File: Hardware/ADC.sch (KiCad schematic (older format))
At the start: 9 parts, among them U2 NCP51460SN33T1G, U3 MCP3002

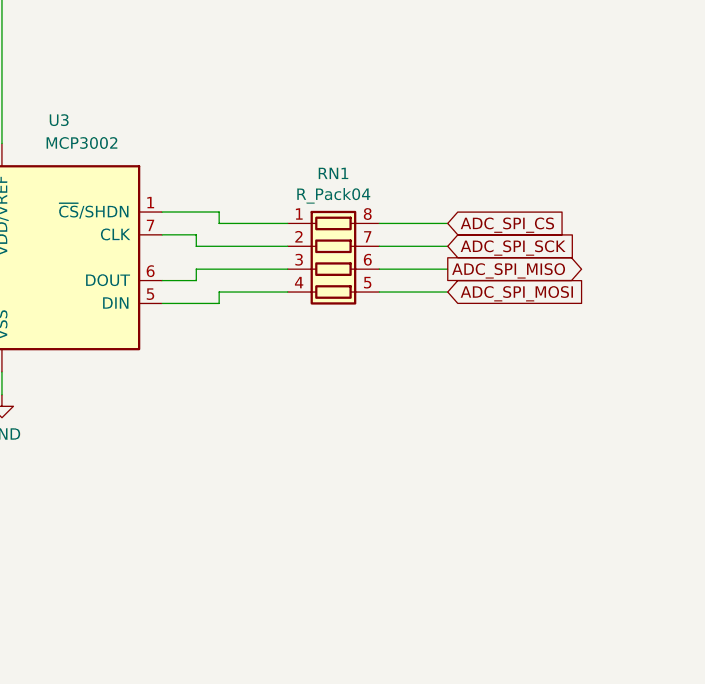
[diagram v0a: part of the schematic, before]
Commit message: [Hardware] Replaced in schematic hard to find resistors array using 2012 package by classic 1206 discrete resistors.
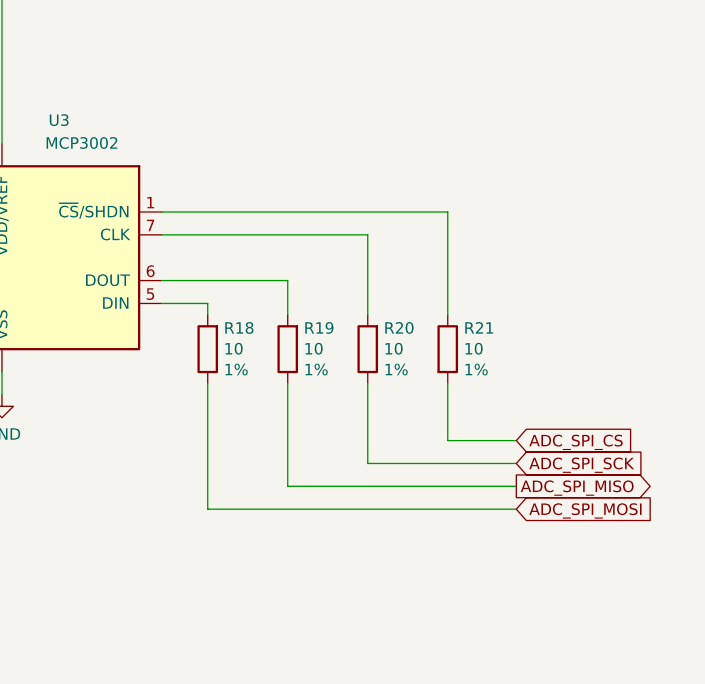
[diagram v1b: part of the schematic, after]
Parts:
- removed RN1: R_Pack04, Resistor_SMD:R_Array_Convex_4x1206, symbol Device:R_Pack04
- added R18, R19, R20, R21: 10, Resistor_SMD:R_1206_3216Metric_Pad1.42x1.75mm_HandSolder, symbol Device:R
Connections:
- net ADC_SPI_CS: now also R21.2
- net ADC_SPI_MISO: now also R19.1
- net ADC_SPI_MOSI: now also R18.1
- net ADC_SPI_SCK: now also R20.1
- net at U3.1 (~CS~/SHDN): now also R21.1
- net at U3.7 (CLK): now also R20.2
- net at U3.6 (DOUT): now also R19.2
- net at U3.5 (DIN): now also R18.2
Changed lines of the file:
@@
 Wire Wire Line
 	6000 4200 6000 4100
-Text GLabel 7950 3450 2    50   Input ~ 0
+Text GLabel 8250 4400 2    50   Input ~ 0
 ADC_SPI_CS
-Text GLabel 7950 3550 2    50   Input ~ 0
+Text GLabel 8250 4500 2    50   Input ~ 0
 ADC_SPI_SCK
-Text GLabel 7950 3650 2    50   Output ~ 0
+Text GLabel 8250 4600 2    50   Output ~ 0
 ADC_SPI_MISO
-Text GLabel 7950 3750 2    50   Input ~ 0
+Text GLabel 8250 4700 2    50   Input ~ 0
 ADC_SPI_MOSI
 $Comp
@@
 Wire Wire Line
 	3700 5250 3700 5200
-$Comp
-L Device:R_Pack04 RN1
-U 1 1 5F207575
-P 7450 3650
-F 0 "RN1" V 7033 3650 50  0000 C CNN
-F 1 "R_Pack04" V 7124 3650 50  0000 C CNN
-F 2 "Resistor_SMD:R_Array_Convex_4x1206" V 7725 3650 50  0001 C CNN
-F 3 "~" H 7450 3650 50  0001 C CNN
-F 4 "MP000987" V 7450 3650 50  0001 C CNN "Value2"
-F 5 "Multicomp" V 7450 3650 50  0001 C CNN "Manufacturer"
-	1    7450 3650
-	0    1    1    0
-$EndComp
-Wire Wire Line
-	6700 3700 6850 3700
-Wire Wire Line
-	6850 3700 6850 3650
-Wire Wire Line
-	6850 3650 7250 3650
-Wire Wire Line
-	6950 3800 6950 3750
-Wire Wire Line
-	6950 3750 7250 3750
-Wire Wire Line
-	6700 3800 6950 3800
-Wire Wire Line
-	6700 3500 6850 3500
-Wire Wire Line
-	6850 3500 6850 3550
-Wire Wire Line
-	6850 3550 7250 3550
-Wire Wire Line
-	6700 3400 6950 3400
-Wire Wire Line
-	6950 3400 6950 3450
-Wire Wire Line
-	6950 3450 7250 3450
-Wire Wire Line
-	7650 3750 7950 3750
-Wire Wire Line
-	7650 3650 7950 3650
-Wire Wire Line
-	7650 3550 7950 3550
-Wire Wire Line
-	7650 3450 7950 3450
 Text GLabel 3650 5450 0    50   UnSpc ~ 0
 FRONT_BOARD_LDR
@@
 Wire Wire Line
 	3700 5250 3700 5450
+$Comp
+L Device:R R19
+U 1 1 5F47E9CC
+P 7250 4000
+F 0 "R19" H 7180 3909 50  0000 R CNN
+F 1 "10" H 7180 4000 50  0000 R CNN
+F 2 "Resistor_SMD:R_1206_3216Metric_Pad1.42x1.75mm_HandSolder" V 7180 4000 50  0001 C CNN
+F 3 "~" H 7250 4000 50  0001 C CNN
+F 4 "1%" H 7180 4091 50  0000 R CNN "Value2"
+	1    7250 4000
+	-1   0    0    1
+$EndComp
+$Comp
+L Device:R R20
+U 1 1 5F47ECFD
+P 7600 4000
+F 0 "R20" H 7530 3909 50  0000 R CNN
+F 1 "10" H 7530 4000 50  0000 R CNN
+F 2 "Resistor_SMD:R_1206_3216Metric_Pad1.42x1.75mm_HandSolder" V 7530 4000 50  0001 C CNN
+F 3 "~" H 7600 4000 50  0001 C CNN
+F 4 "1%" H 7530 4091 50  0000 R CNN "Value2"
+	1    7600 4000
+	-1   0    0    1
+$EndComp
+$Comp
+L Device:R R21
+U 1 1 5F47F244
+P 7950 4000
+F 0 "R21" H 8020 4091 50  0000 L CNN
+F 1 "10" H 8020 4000 50  0000 L CNN
+F 2 "Resistor_SMD:R_1206_3216Metric_Pad1.42x1.75mm_HandSolder" V 7880 4000 50  0001 C CNN
+F 3 "~" H 7950 4000 50  0001 C CNN
+F 4 "1%" H 8020 3909 50  0000 L CNN "Value2"
+	1    7950 4000
+	1    0    0    -1
+$EndComp
+$Comp
+L Device:R R18
+U 1 1 5F47B7CA
+P 6900 4000
+F 0 "R18" H 6830 3909 50  0000 R CNN
+F 1 "10" H 6830 4000 50  0000 R CNN
+F 2 "Resistor_SMD:R_1206_3216Metric_Pad1.42x1.75mm_HandSolder" V 6830 4000 50  0001 C CNN
+F 3 "~" H 6900 4000 50  0001 C CNN
+F 4 "1%" H 6830 4091 50  0000 R CNN "Value2"
+	1    6900 4000
+	-1   0    0    1
+$EndComp
+Wire Wire Line
+	6700 3800 6900 3800
+Wire Wire Line
+	6900 3800 6900 3850
+Wire Wire Line
+	7250 3700 7250 3850
+Wire Wire Line
+	6700 3700 7250 3700
+Wire Wire Line
+	6700 3500 7600 3500
+Wire Wire Line
+	7600 3500 7600 3850
+Wire Wire Line
+	6700 3400 7950 3400
+Wire Wire Line
+	7950 3400 7950 3850
+Wire Wire Line
+	7950 4150 7950 4400
+Wire Wire Line
+	7950 4400 8250 4400
+Wire Wire Line
+	7600 4500 8250 4500
+Wire Wire Line
+	7600 4150 7600 4500
+Wire Wire Line
+	7250 4150 7250 4600
+Wire Wire Line
+	7250 4600 8250 4600
+Wire Wire Line
+	8250 4700 6900 4700
+Wire Wire Line
+	6900 4700 6900 4150
 $EndSCHEMATC
